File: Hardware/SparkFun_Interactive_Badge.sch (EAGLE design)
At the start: 35 parts, among them Q1 DMG2307L, U1 MIC5205-3.3V, U2 ATMEGA328P, U3 CY7C65213, Y1 4MHz

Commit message: Updated to v10
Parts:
- FRAME1: VERSION (none) -> v10
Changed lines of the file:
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@@
 <part name="FRAME1" library="SparkFun-Aesthetics" deviceset="FRAME-LETTER" device="">
 <attribute name="DESIGNER" value="Shawn Hymel"/>
+<attribute name="VERSION" value="v10"/>
 </part>
 <part name="FID1" library="SparkFun-Aesthetics" deviceset="FIDUCIAL" device="1X2"/>

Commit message: More re-routing for v11 of the BadgerStick.
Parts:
- removed JP4: M15LOCK_NO_SILK, SparkFun-Connectors:M15LOCK_NO_SILK
- added J1: (no value), SparkFun-Connectors:JST_2MM_MALE
- added JP2: (no value), SparkFun-Connectors:M15LOCK_NO_SILK
- added R5, R6: 1K, SparkFun-Resistors:1KOHM-1/10W-1%(0603)
- FRAME1: VERSION v10 -> v11
- JP3: value M15LOCK_NO_SILK -> (none); device SparkFun-Connectors:M15LOCK_NO_SILK -> SparkFun-Connectors:M12LOCK_NO_SILK
- U2: value ATMEGA328P -> ATMEGA328P_TQFP; device SparkFun-DigitalIC:ATMEGA328_SMT -> SparkFun-DigitalIC:ATMEGA328P_TQFP
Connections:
- new net N$3: R5.1, U3.TXD
- new net N$7: R6.1, U3.RXD
- net 3.3V: now also JP2.14; no longer JP4.2
- net 5V: now also JP2.15; no longer JP4.1
- net A0: now also JP3.8; no longer JP4.11
- net A1: now also JP3.7; no longer JP4.10
- net A2: now also JP3.6; no longer JP4.9
- net A3: now also JP3.5; no longer JP4.8
- net A4: now also JP3.4; no longer JP4.7
- net A5: now also JP3.3; no longer JP4.6
- net D10: now also JP3.12; no longer JP4.15, JP6.1
- net D2: now also JP2.8; no longer JP3.8
- net D3: now also JP2.7; no longer JP3.7
- net D4: now also JP2.6; no longer JP3.6
- net D5: now also JP2.5; no longer JP3.5
- net D6: now also JP2.4; no longer JP3.4
- net D7: now also JP2.3; no longer JP3.3
- net D8: now also JP2.2; no longer JP3.2
- net D9: now also JP2.1; no longer JP3.1
- net DTR: now also JP2.13; no longer JP3.13
- net GND: now also J1.-, JP2.9, JP3.2, U2.GND@3, U2.GND@5; no longer JP3.14, JP3.9, JP4.3, U2.GND@1, U2.GND@2
- net MISO: now also JP3.10; no longer JP4.13
- net MOSI: now also JP3.11; no longer JP4.14, JP6.3
- net RESET: now also JP2.10; no longer JP3.10, JP4.4
- net RXI: now also JP2.11, JP6.1, R5.2; no longer JP3.11, U3.TXD
- net SCK: now also JP3.9; no longer JP4.12
- net TXO: now also JP2.12, JP6.3, R6.2; no longer JP3.12, U3.RXD
- net VBAT: now also J1.+; no longer JP3.15
- net VCC: now also JP3.1, U2.VCC@4, U2.VCC@6; no longer JP4.5, U2.VCC@1, U2.VCC@2
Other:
- note added: "Battery Connector"
- note added: "Game Port"
- note added: "RX (Pin 0)"
- note added: "TX (Pin 1)"
- note removed: "RX (Pin 10)"
- note removed: "Software Serial"
- note removed: "TX (Pin 11)"
- moved on the sheet: C7, C8, U3

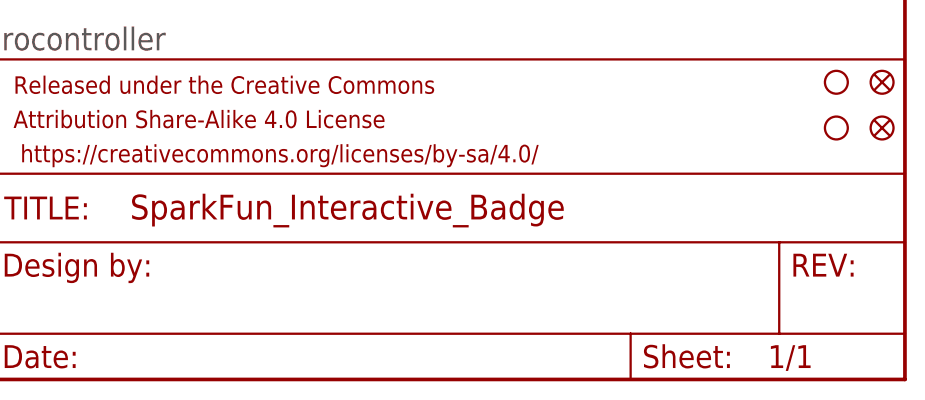
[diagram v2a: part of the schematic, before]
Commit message: Adjusted vias to allow for 2 connections to GND from 328p. Moved silk slightly to avoid vias (as possible).
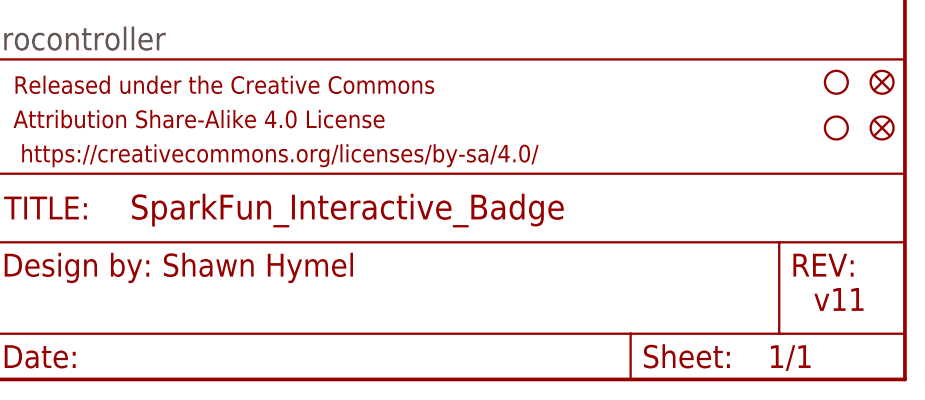
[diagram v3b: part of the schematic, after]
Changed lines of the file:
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@@
 </plain>
 <instances>
-<instance part="FRAME1" gate="G$1" x="0" y="0"/>
+<instance part="FRAME1" gate="G$1" x="0" y="0">
+<attribute name="DESIGNER" x="166.37" y="11.43" size="2.54" layer="94"/>
+<attribute name="VERSION" x="238.76" y="7.62" size="2.54" layer="94"/>
+</instance>
 <instance part="FRAME1" gate="V" x="147.32" y="0"/>
 <instance part="FID1" gate="G$1" x="246.38" y="33.02"/>

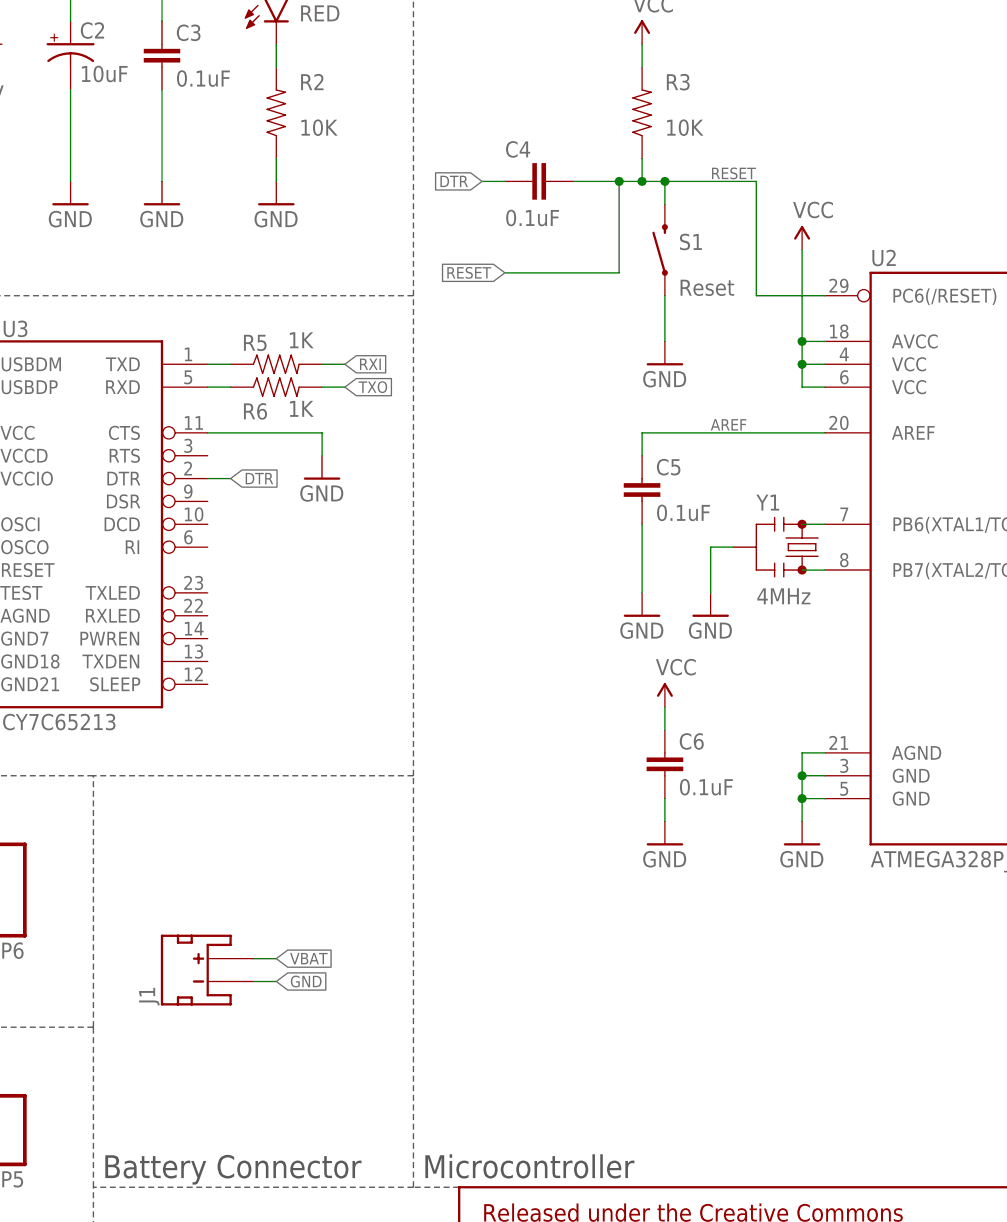
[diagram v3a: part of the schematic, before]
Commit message: Changed LED silk to '13'. Added notes to sch about voltage range and JST connector. Moved wire in sch for VCC on 328p to avoid confusion with the RESET line.
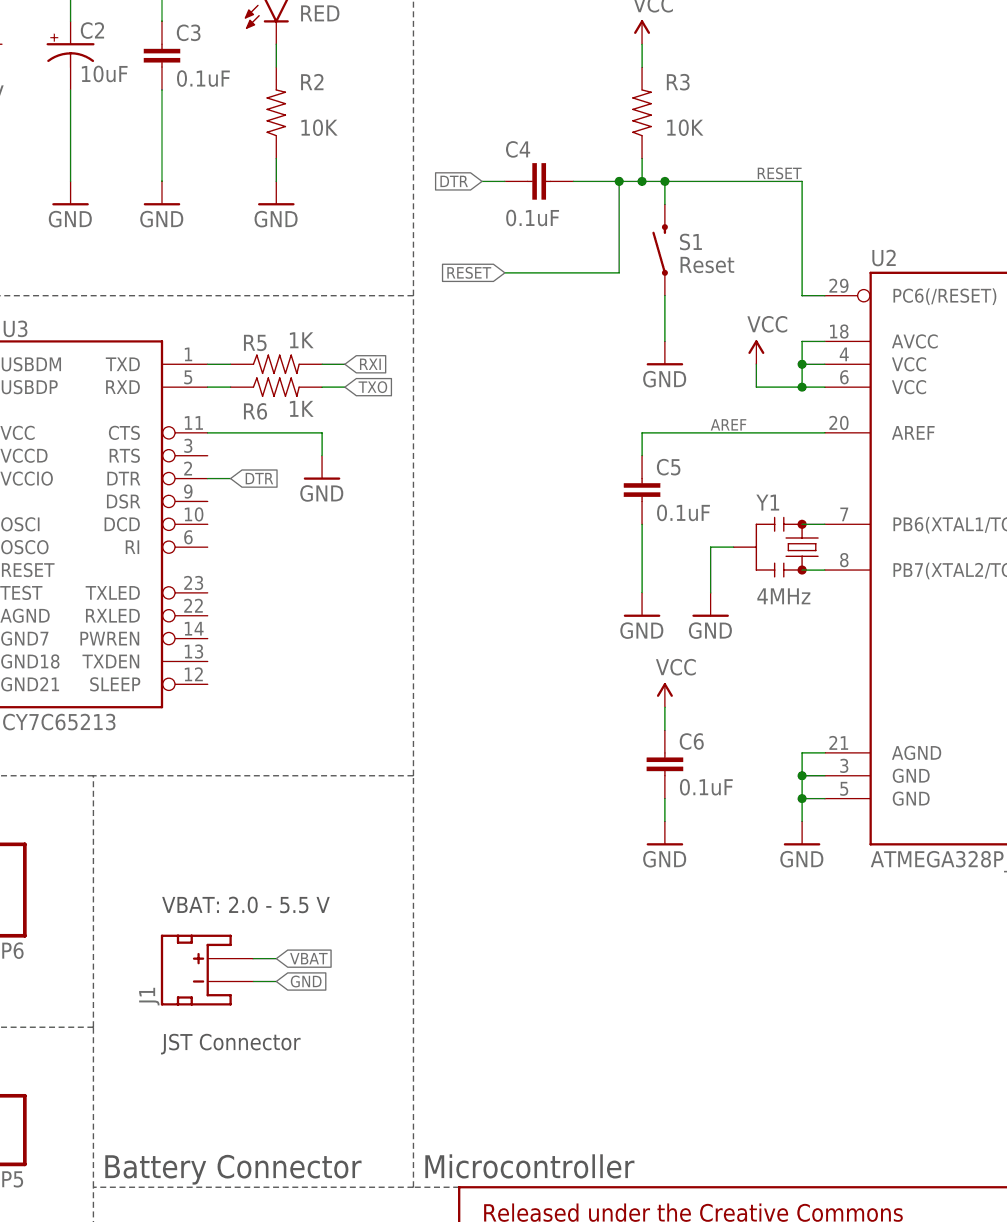
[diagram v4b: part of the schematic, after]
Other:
- note added: "JST Connector"
- note added: "VBAT: 2.0 - 5.5 V"
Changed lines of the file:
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@@
 <text x="143.256" y="36.576" size="2.54" layer="97">Microcontroller</text>
 <text x="107.696" y="36.576" size="2.54" layer="97">Battery Connector</text>
+<text x="114.3" y="66.04" size="1.778" layer="97">VBAT: 2.0 - 5.5 V</text>
+<text x="114.3" y="50.8" size="1.778" layer="97">JST Connector</text>
 </plain>
 <instances>
@@
 <instance part="S1" gate="G$1" x="170.18" y="139.7" smashed="yes" rot="R90">
 <attribute name="NAME" x="171.704" y="139.7" size="1.778" layer="95"/>
-<attribute name="FUNC" x="171.704" y="134.62" size="1.778" layer="96"/>
+<attribute name="FUNC" x="171.704" y="137.16" size="1.778" layer="96"/>
 </instance>
 <instance part="R3" gate="G$1" x="167.64" y="154.94" smashed="yes" rot="R90">
@@
 </instance>
 <instance part="SUPPLY6" gate="G$1" x="167.64" y="162.56"/>
-<instance part="SUPPLY7" gate="G$1" x="185.42" y="139.7"/>
+<instance part="SUPPLY7" gate="G$1" x="180.34" y="127"/>
 <instance part="C5" gate="G$1" x="167.64" y="111.76"/>
 <instance part="GND8" gate="1" x="170.18" y="127"/>
@@
 <segment>
 <pinref part="SUPPLY7" gate="G$1" pin="VCC"/>
-<wire x1="185.42" y1="139.7" x2="185.42" y2="129.54" width="0.1524" layer="91"/>
+<wire x1="180.34" y1="127" x2="180.34" y2="124.46" width="0.1524" layer="91"/>
 <pinref part="U2" gate="U$1" pin="VCC@6"/>
 <wire x1="185.42" y1="129.54" x2="185.42" y2="127" width="0.1524" layer="91"/>
@@
 <pinref part="U2" gate="U$1" pin="AVCC"/>
 <wire x1="187.96" y1="129.54" x2="185.42" y2="129.54" width="0.1524" layer="91"/>
-<junction x="185.42" y="129.54"/>
+<wire x1="180.34" y1="124.46" x2="185.42" y2="124.46" width="0.1524" layer="91"/>
+<junction x="185.42" y="124.46"/>
 </segment>
 <segment>
@@
 <segment>
 <pinref part="U2" gate="U$1" pin="PC6(/RESET)"/>
-<wire x1="187.96" y1="134.62" x2="180.34" y2="134.62" width="0.1524" layer="91"/>
-<wire x1="180.34" y1="134.62" x2="180.34" y2="147.32" width="0.1524" layer="91"/>
-<wire x1="180.34" y1="147.32" x2="170.18" y2="147.32" width="0.1524" layer="91"/>
+<wire x1="187.96" y1="134.62" x2="185.42" y2="134.62" width="0.1524" layer="91"/>
+<wire x1="185.42" y1="134.62" x2="185.42" y2="147.32" width="0.1524" layer="91"/>
+<wire x1="185.42" y1="147.32" x2="170.18" y2="147.32" width="0.1524" layer="91"/>
 <junction x="170.18" y="147.32"/>
 <pinref part="S1" gate="G$1" pin="2"/>
@@
 <pinref part="C4" gate="G$1" pin="2"/>
 <wire x1="160.02" y1="147.32" x2="165.1" y2="147.32" width="0.1524" layer="91"/>
-<label x="175.26" y="147.574" size="1.27" layer="95"/>
+<label x="180.34" y="147.574" size="1.27" layer="95"/>
 <pinref part="R3" gate="G$1" pin="1"/>
 <wire x1="165.1" y1="147.32" x2="167.64" y2="147.32" width="0.1524" layer="91"/>
